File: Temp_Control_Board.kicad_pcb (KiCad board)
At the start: 4 copper layers, 50.8 x 53.3 mm, 50 parts, among them J1 OVEN_INTERFACE, J2 OLED, J3 USB_B_Micro, J4 MICROSD, J5 BREAKOUT, Q1 BC847BS, SW1 BOOT, SW2 EN, U1 ESP-WROOM-32, U2 AZ1117EH-3.3TRG1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

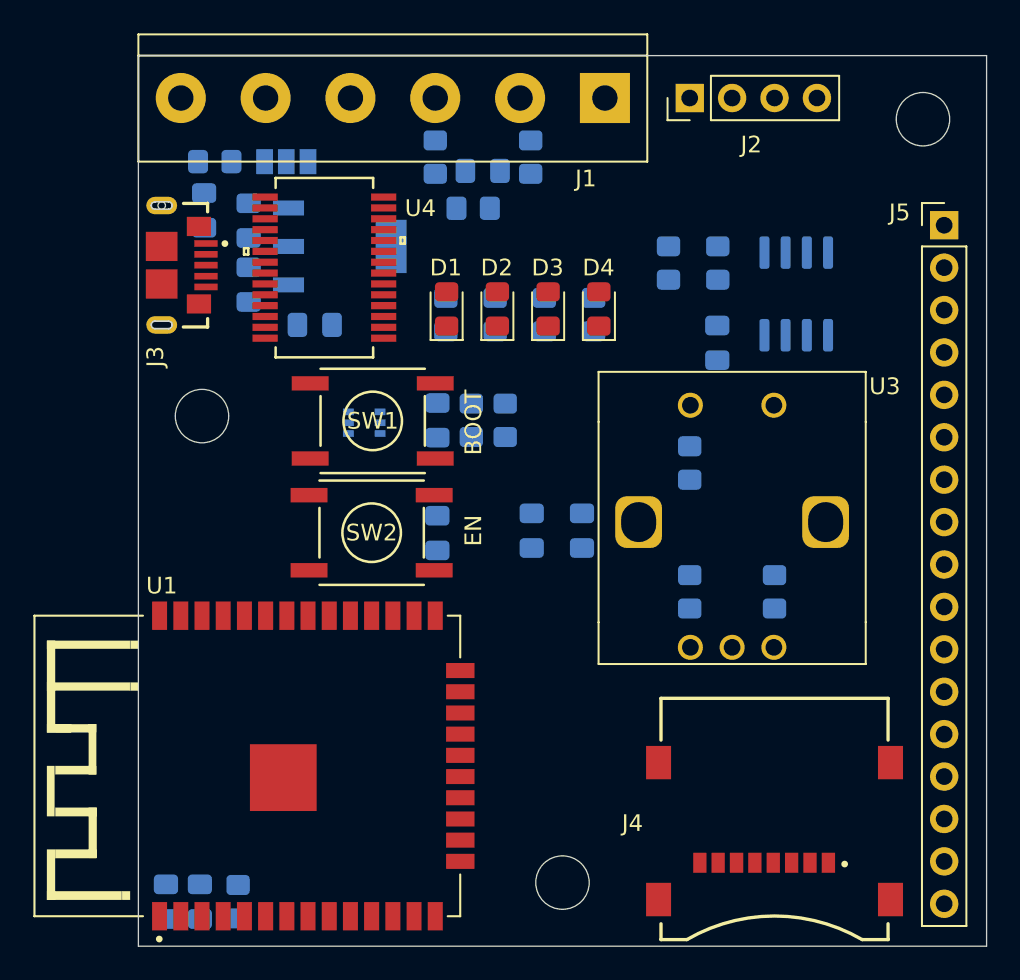
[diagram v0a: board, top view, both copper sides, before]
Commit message: pcb: began routing
    - Updated ESP32 part to new KiCAD version
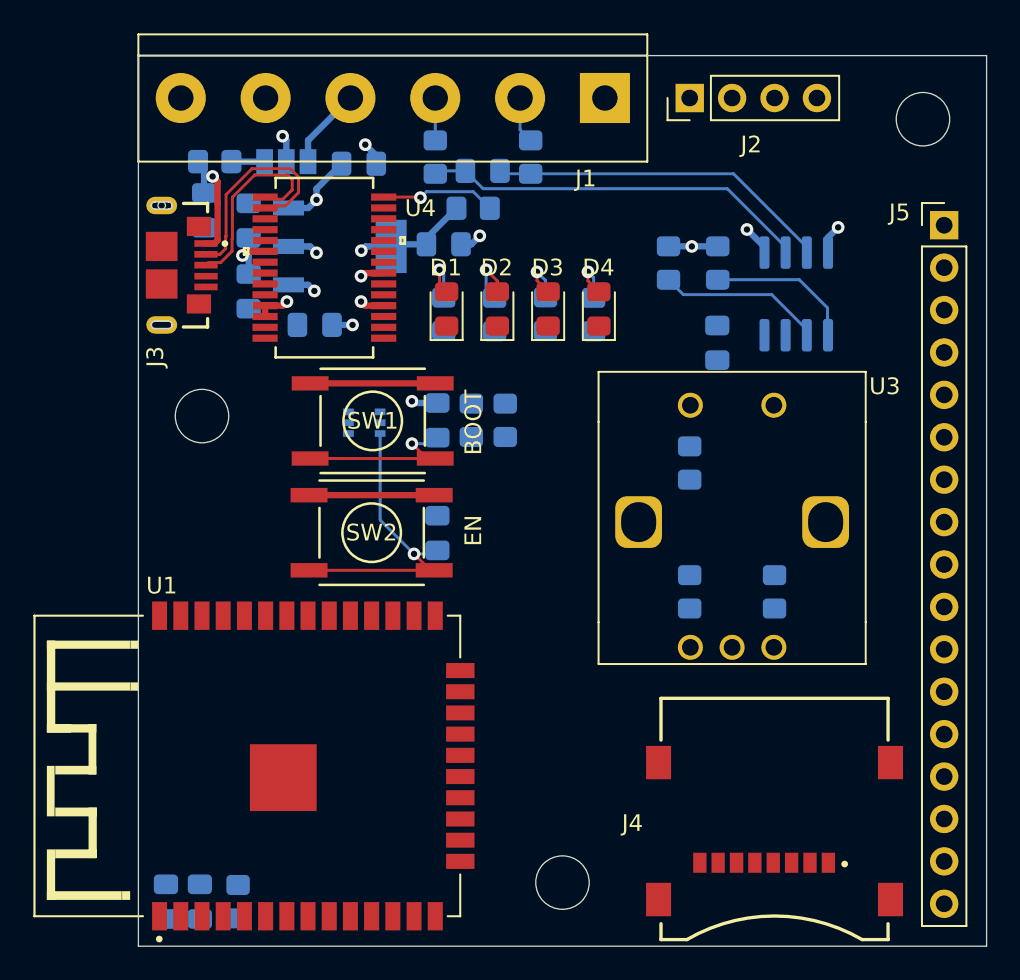
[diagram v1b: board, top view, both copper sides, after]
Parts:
- moved C3 24.3 mm to (89.4, 105.5), turned to 0 degrees
- moved C4 19.0 mm to (94.5, 110.4), turned to 0 degrees
- moved R10 8.98 mm to (94.5, 114.6)
- moved R13 8.85 mm to (103.5, 114.6)
- moved R12 3.02 mm to (100.6, 114.5)
- moved R11 2.98 mm to (97.5, 114.6)
- moved C7 0.40 mm to (82.8, 113.2)
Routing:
- net GND: track 0.00 -> 27.5 mm, vias 0 -> 8
- net MAX_TX-: track 0.00 -> 23.3 mm
- net MAX_TC+: track 0.00 -> 20.6 mm
- net EN: track 0.00 -> 18.6 mm, vias 0 -> 1
- net +3V3: track 0.00 -> 15.0 mm, vias 0 -> 5
- net /D-: track 0.00 -> 13.1 mm
- net /D+: track 0.00 -> 11.9 mm
- net BOOT: track 0.00 -> 10.9 mm, vias 0 -> 1
- net +5V: track 0.00 -> 10.7 mm, vias 0 -> 3
- net MAX_CSN: track 0.00 -> 9.86 mm
- net MAX_SCK: track 0.00 -> 8.92 mm
- net /VBUS: track 0.00 -> 7.32 mm, vias 0 -> 1
- net FT_PWREN: track 0.00 -> 6.93 mm, vias 0 -> 1
- net VCONN: track 0.00 -> 4.86 mm
- net Net-(D2-A): track 0.00 -> 3.49 mm, vias 0 -> 1
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- added copper zone on In2.Cu, net +3V3
- added copper zone on In2.Cu, net +5V

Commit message: simple routing complete
    - Mostly North/South on front Copper, mostly East/West on Back
      Copper
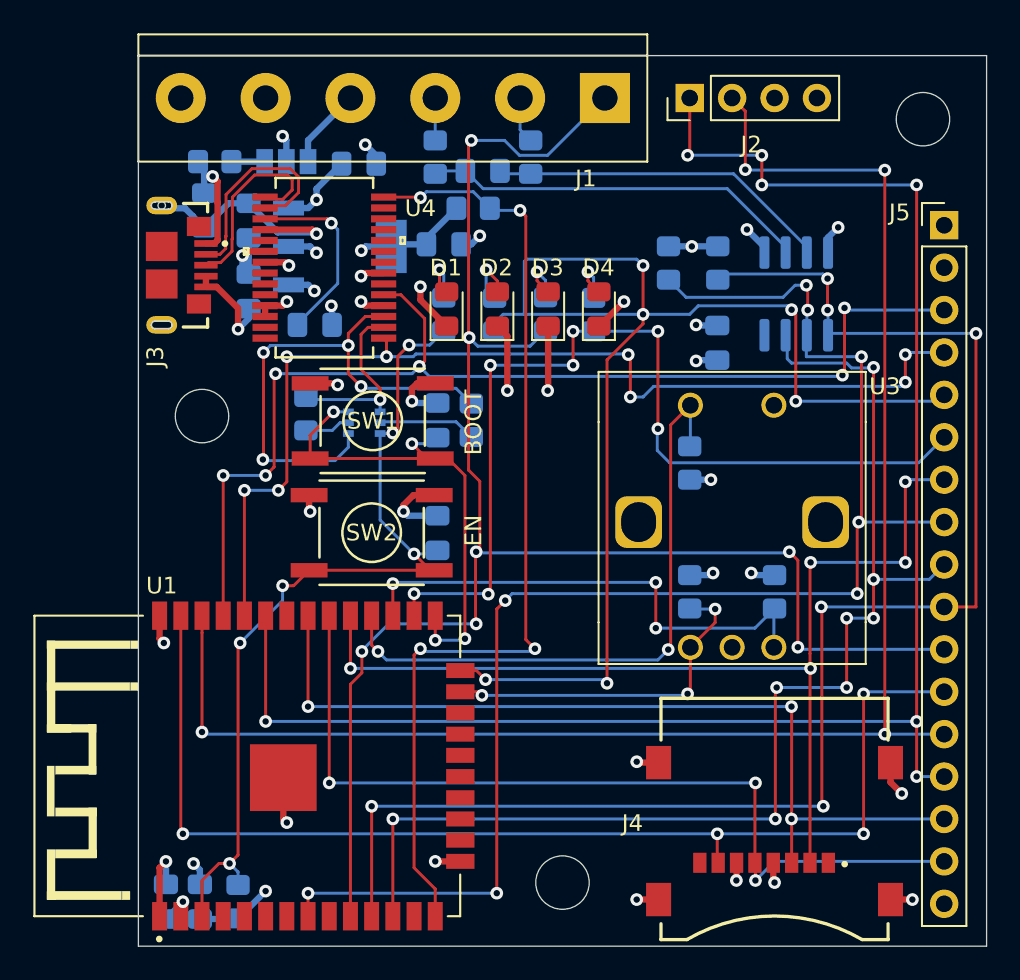
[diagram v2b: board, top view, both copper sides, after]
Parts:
- moved R8 11.9 mm to (86.2, 120.5), turned to -90 degrees
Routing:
- net RELAY+: track 0.00 -> 101.7 mm, vias 0 -> 7
- net OLED_SDA: track 0.00 -> 101.4 mm, vias 0 -> 7
- net OLED_SCL: track 0.00 -> 98.2 mm, vias 0 -> 4
- net MAX_SCK: track 8.92 -> 90.5 mm, vias 0 -> 6
- net LED_ESP0: track 0.00 -> 79.0 mm, vias 0 -> 6
- net MAX_CSN: track 9.86 -> 87.7 mm, vias 0 -> 8
- net MAX_SO: track 0.00 -> 73.1 mm, vias 0 -> 8
- net SD_DO: track 0.00 -> 68.9 mm, vias 0 -> 4
- net FT_RX: track 0.00 -> 67.8 mm, vias 0 -> 6
- net FT_TX: track 0.00 -> 62.9 mm, vias 0 -> 8
- net SD_CS: track 0.00 -> 61.6 mm, vias 0 -> 5
- net LED_ESP1: track 0.00 -> 56.9 mm, vias 0 -> 7
- net SD_SCK: track 0.00 -> 53.2 mm, vias 0 -> 3
- net SD_DI: track 0.00 -> 52.9 mm, vias 0 -> 3
- net FT_PWREN: track 6.93 -> 59.1 mm, vias 1 -> 4
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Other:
- board text added: "Todo: Route all bottom signals East/West and All Top North/South"

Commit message: pcb: Finished routing
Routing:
- net MAX_CSN: track 87.7 -> 81.5 mm, vias 8 -> 6
- net MAX_SCK: track 90.5 -> 84.3 mm, vias 6 -> 3
- net OLED_SDA: track 101.4 -> 95.9 mm, vias 7 -> 3
- net RELAY+: track 101.7 -> 97.6 mm, vias 7 -> 5
- net BOOT: track 30.5 -> 26.5 mm, vias 4 -> 2
- net FT_RX: track 67.8 -> 64.0 mm, vias 6 -> 4
- net SD_CS: track 61.6 -> 58.1 mm
- net OLED_SCL: track 98.2 -> 95.0 mm, vias 4 -> 2
- net MAX_SO: track 73.1 -> 69.9 mm, vias 8 -> 6
- net FT_TX: track 62.9 -> 60.2 mm, vias 8 -> 4
- net LED_ESP0: track 79.0 -> 76.3 mm
- net FT_PWREN: track 59.1 -> 56.6 mm
- net SD_DO: track 68.9 -> 66.7 mm
- net SD_SCK: track 53.2 -> 51.4 mm
- net ROT_CHA: track 21.0 -> 19.3 mm
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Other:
- rule pad_to_mask_clearance: 0.05 -> 0
- board text removed: "Todo: Route all bottom signals East/West and All Top North/South"
